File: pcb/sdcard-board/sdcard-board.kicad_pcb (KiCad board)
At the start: 2 copper layers, 82.5 x 67.3 mm, 38 parts, among them J3 SD Card Board, J4 EXPBUS1, U1 74HC123, U3 74HC00, U4 74HC00, U5 74HC163, U6 74HC00, U7 74HC165, U8 74HC595, X1 16MHz

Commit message: Further redesigning boards
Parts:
- removed J4: EXPBUS1, Connector_PinHeader_2.54mm:PinHeader_2x20_P2.54mm_Vertical
- removed REF**: OSHW-Logo2_7.3x6mm_SilkScreen, Symbol:OSHW-Logo2_7.3x6mm_SilkScreen
- added C13: 0.1uF, Capacitor_THT:C_Disc_D5.0mm_W2.5mm_P5.00mm, F.Cu at (74.9, 115.6)
- added J1: EXPBUS2, Connector_PinSocket_2.54mm:PinSocket_2x20_P2.54mm_Horizontal, F.Cu at (45.7, 141.7)
- added U10: 74HC138, Package_DIP:DIP-16_W7.62mm_Socket, F.Cu at (78.7, 134.6)
- added U9: 74HC688, Package_DIP:DIP-20_W7.62mm_Socket, F.Cu at (45.7, 134.6)
- C3: value 220uF -> 0.1uF; footprint Capacitor_THT:CP_Radial_D6.3mm_P2.50mm -> Capacitor_THT:C_Disc_D5.0mm_W2.5mm_P5.00mm
- J3: footprint Connector_PinSocket_2.54mm:PinSocket_1x06_P2.54mm_Vertical -> sdcard-holder:sdcard-socket
- TP5, TP6, TP7, TP8: footprint TestPoint:TestPoint_Pad_4.0x4.0mm -> TestPoint:TestPoint_THTPad_2.5x2.5mm_Drill1.2mm
- moved C3 87.7 mm to (74.3, 128.3), turned to -90 degrees
- moved J3 80.0 mm to (118.7, 115.6)
- moved C8 77.2 mm to (40.6, 128.3), turned to -90 degrees
- moved TP8 69.6 mm to (95.9, 68.6)
- moved C12 68.3 mm to (74.9, 102.9), turned to -90 degrees
- moved R1 67.3 mm to (58.4, 109.2), turned to 180 degrees
- moved X1 65.1 mm to (41.9, 119.4), turned to 90 degrees
- moved TP2 53.7 mm to (95.8, 60.3)
- moved TP7 51.2 mm to (80.6, 68.6)
- moved TP1 49.1 mm to (80.6, 60.3)
- moved C4 47.8 mm to (40.6, 69.8), turned to 180 degrees
- moved U3 43.4 mm to (78.7, 96.5)
- moved R2 41.3 mm to (41.9, 74.4), turned to 180 degrees
- moved U4 41.0 mm to (78.7, 109.2)
- moved U8 40.4 mm to (50.8, 121.9)
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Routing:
- net GND: track 0.00 -> 735.7 mm
- net VCC: track 0.00 -> 604.3 mm
- net CLK: track 0.00 -> 204.3 mm, vias 0 -> 2
- net ~{CS}: track 0.00 -> 130.1 mm, vias 0 -> 1
- net MISO: track 0.00 -> 122.4 mm, vias 0 -> 1
- net D2: track 0.00 -> 115.9 mm
- net D1: track 0.00 -> 109.6 mm, vias 0 -> 2
- net D5: track 0.00 -> 101.2 mm
- net Net-(D1-K): track 0.00 -> 97.5 mm, vias 0 -> 1
- net D3: track 0.00 -> 89.0 mm, vias 0 -> 1
- net MOSI: track 0.00 -> 89.0 mm, vias 0 -> 1
- net D0: track 0.00 -> 85.9 mm
- net D6: track 0.00 -> 84.2 mm
- net D7: track 0.00 -> 83.4 mm
- net D4: track 0.00 -> 76.7 mm
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- added copper zone on F.Cu, net GND
- added copper zone on B.Cu, net VCC
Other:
- board size 82.5 x 67.3 mm -> 96.5 x 94 mm

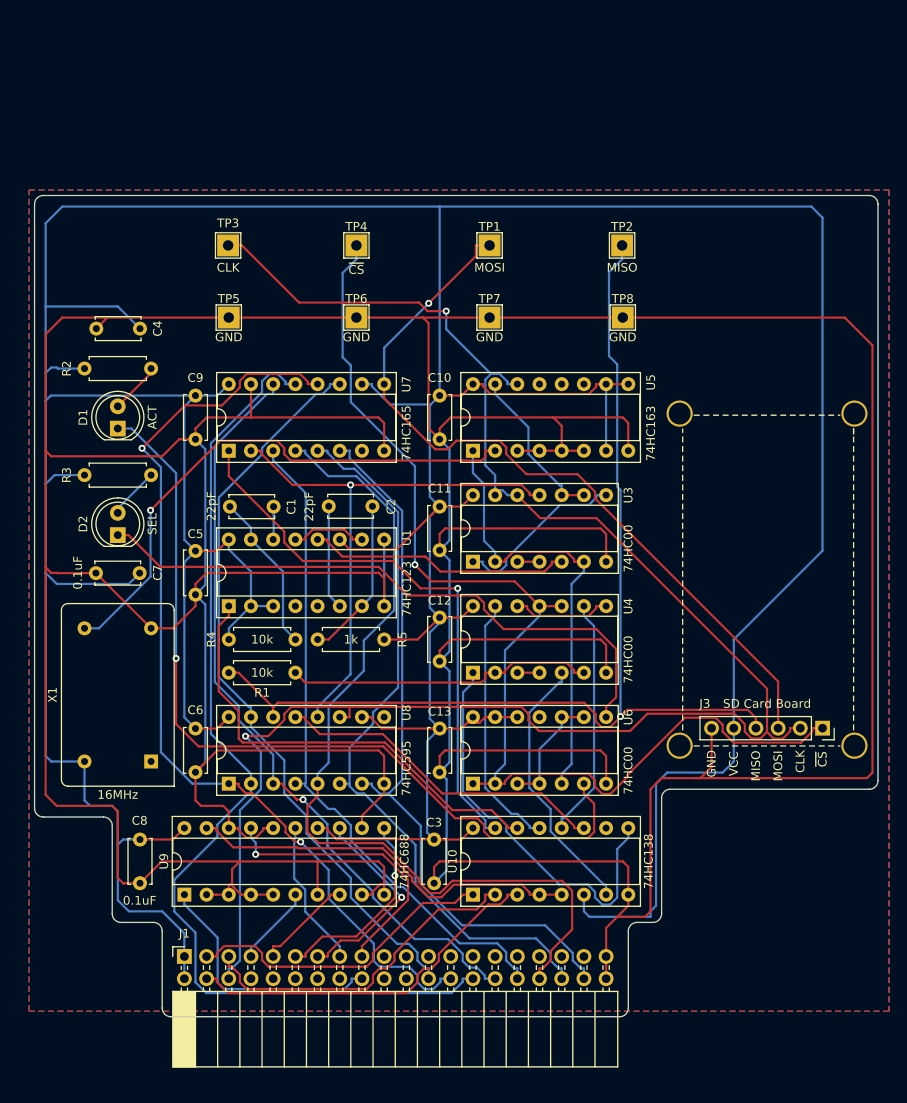
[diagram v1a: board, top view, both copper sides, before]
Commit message: Revising SDCARD board
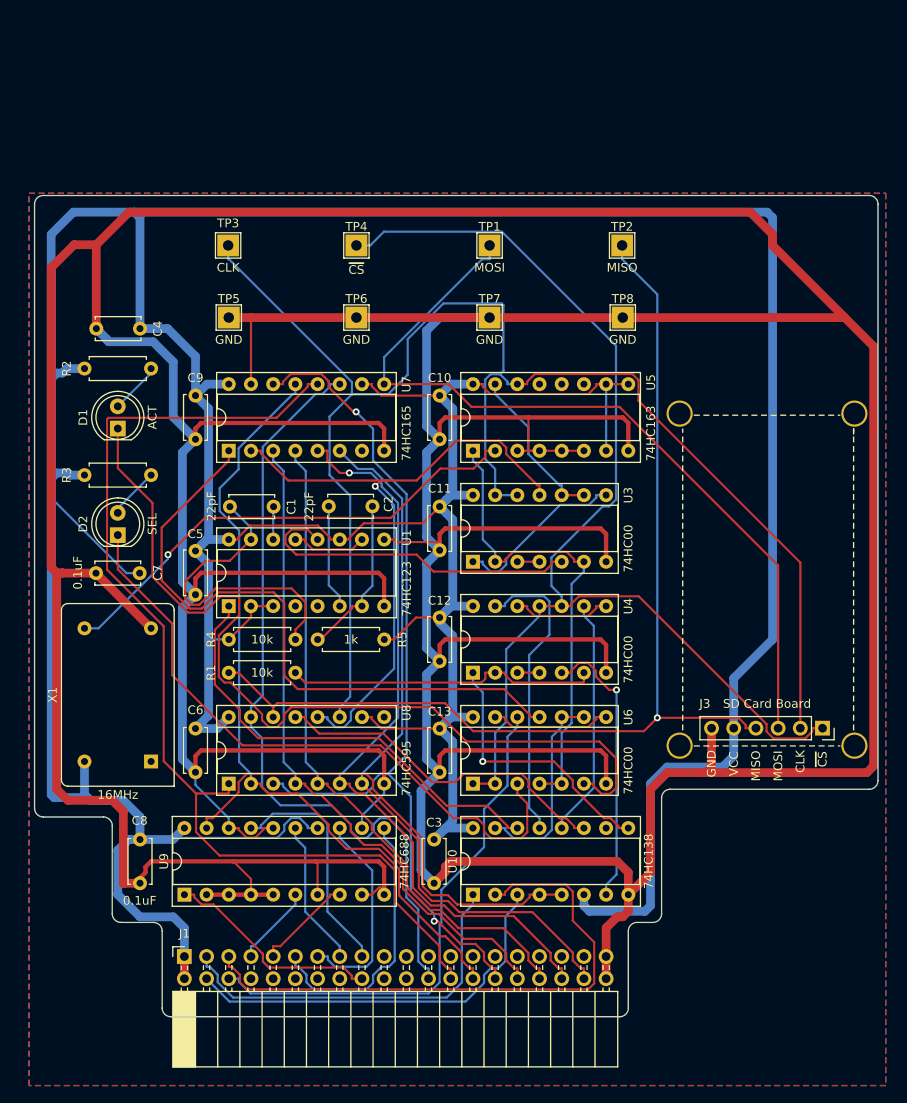
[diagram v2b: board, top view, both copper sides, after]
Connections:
- net ~{CLK} renamed ~{SDCLK}
- J3 pad 2: CLK -> SDCLK
- TP3 pad 1: CLK -> SDCLK
- U3 pad 12: CLK -> SDCLK
- U3 pad 13: CLK -> SDCLK
- U5 pad 14: CLK -> SDCLK
- U6 pad 10: Net-(U6-Pad10) -> ~{SER_WR}
- U6 pad 11: unconnected-(U6-Pad11) -> Net-(U7-~{PL})
- U6 pad 12: VCC -> CLK
- U6 pad 13: VCC -> Net-(U6-Pad13)
- U6 pad 3: Net-(U6-Pad10) -> Net-(D2-K)
- U6 pad 4: Net-(U6-Pad10) -> SD_SPI
- U6 pad 8: Net-(D2-K) -> Net-(U6-Pad13)
- U6 pad 9: Net-(U6-Pad10) -> ~{SER_WR}
- U7 pad 1: ~{SER_WR} -> Net-(U7-~{PL})
- U8 pad 11: CLK -> SDCLK
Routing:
- net SDCLK: track 0.00 -> 177.7 mm
- net CLK: track 204.3 -> 59.6 mm, vias 2 -> 0
- net GND: track 735.7 -> 824.7 mm
- net Net-(U7-~{PL}): track 0.00 -> 74.3 mm
- net ~{SER_WR}: track 65.0 -> 23.4 mm, vias 1 -> 0
- net A1: track 39.1 -> 66.2 mm
- net D2: track 115.9 -> 89.2 mm
- net VCC: track 604.3 -> 579.7 mm
- net D5: track 101.2 -> 77.0 mm
- net Net-(U1A-RCext): track 18.3 -> 36.4 mm
- net ~{SDOUT_SET}: track 46.7 -> 31.0 mm, vias 0 -> 1
- net Net-(U6-Pad13): track 0.00 -> 13.9 mm
- net Net-(U6-Pad10): track 13.8 -> 0.00 mm
- net D3: track 89.0 -> 102.1 mm, vias 1 -> 2
- net ~{SDCLK}: track 63.6 -> 76.4 mm
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
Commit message: Further revising
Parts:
- added G***: LOGO, components:bytecradle-logo, F.Cu at (113.2, 59.6)
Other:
- board text added: "jlcjlcjlcjlc"
